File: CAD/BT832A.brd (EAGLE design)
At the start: 22.4 x 43.2 mm, 22 parts, among them IC1 CP2102, U2 BT832, U3 LP5907MFX-3.3/NOPB, U4 LP5907MFX-3.3/NOPB, U5 ADS131M08IPBS, X1_8.192MHZ ABM3B-8.000MHZ-B2-T, X2_32.768KHZ FC-12M

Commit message: finished sch
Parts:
- added C10: 1.0uF, adafruit:C0603
- added C11: 0.1uF, adafruit:C0603
- added C12, C13: 1uF, adafruit:C0603
- added D1: BAT60J, diode:SOD323_ST
- added D2, D3: BAS40-06, diode:SOT23
- added LED1, LED2: (no value), adafruit:CHIP-LED0603
- added R1: 4.7kΩ, adafruit:R0603
- added R2, R3: 3.3kΩ, adafruit:R0603
- added R4, R7: 10kΩ, adafruit:R0603
- added R5: 47kΩ, adafruit:R0603
- added R6: 2kΩ, adafruit:R0603
- added U1: MCP73831T-3ACI/OT, MCP73831T-3ACI_OT:SOT95P270X145-5N
- added U6: BCM857BS, BCM857BS:SOT363_NEX
- moved U3 10.4 mm to (22.3, -5.92)
- moved IC1 5.16 mm to (26.5, -19.0)
- moved C1 2.26 mm to (11.0, -7.92)
- moved C2 2.26 mm to (15.1, -7.92)
- moved X2_32.768KHZ 2.26 mm to (13.1, -7.92)
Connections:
- new net +5V: C10.2, C11.2, C7.1, D2.3, IC1.7, IC1.8, U$1.1, U4.1, U4.3, U6.1
- new net 10K: R4.2, U6.2, U6.5, U6.6
- new net B+: D3.3, J1.2
- new net CPRST: IC1.9, R1.1, U2.B5
- new net D+: IC1.4, U$1.3
- new net D-: IC1.5, U$1.2
- new net ID: U$1.4
- new net N$1: LED2.A, R3.1
- new net N$11: LED1.A, R2.2
- new net N$14: D2.2, R5.1, U6.3
- new net N$18: LED1.C, U1.1
- new net N$2: U2.14
- new net N$3: LED2.C
- new net N$4: U2.9
- new net N$5: R3.2
- new net N$8: U3.2
- new net N$9: R6.1, U1.5
- new net NVD: D1.A, D2.1, D3.2, R2.1, R7.2, U1.4, U6.4
- new net RXD: IC1.25, U2.C5
- new net TXD: IC1.26, U2.D5
- new net VBAT: U1.3
- new net VIN: C13.2, D1.C, D3.1, U3.1, U3.3
- new net VSS: U1.2
- net 3V3: no longer C7.1, U4.1, U4.3
- net GND: now also C10.1, C11.1, C12.1, C13.1, J1.1, R4.1, R5.2, R6.2, R7.1, U$1.5; no longer U3.2
- net VDD: now also C12.2, R1.2, U3.5; no longer U2.9

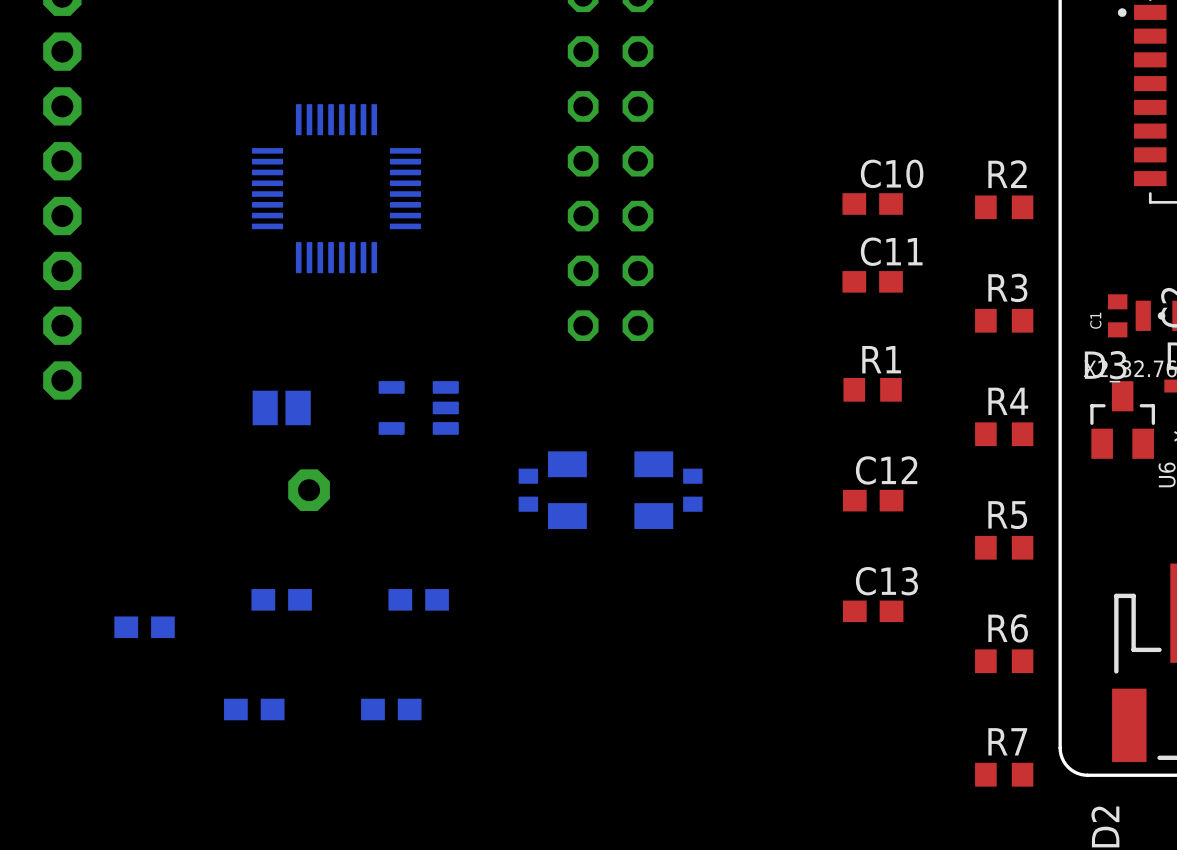
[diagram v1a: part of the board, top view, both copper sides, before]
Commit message: smaller packages
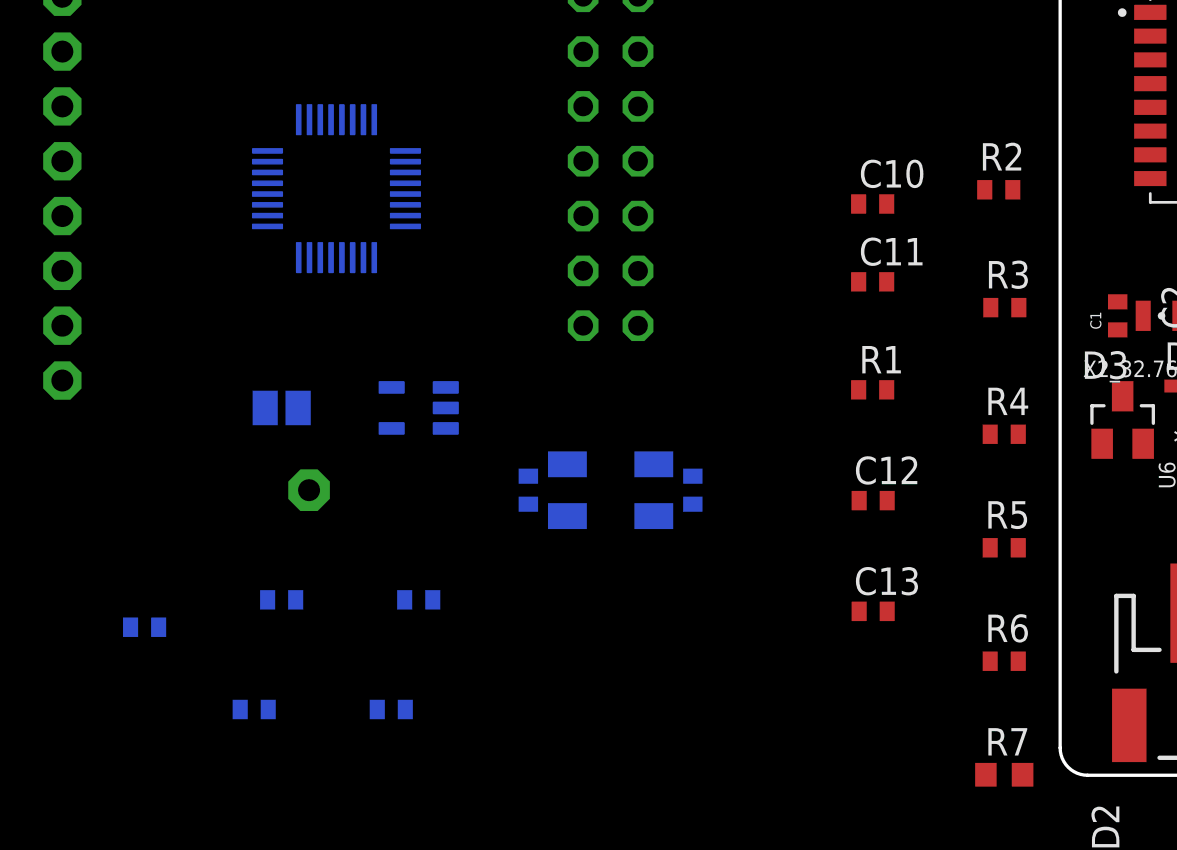
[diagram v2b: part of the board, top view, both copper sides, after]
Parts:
- C10, C11, C12, C13, C5, C6, C7, C8, C9: device adafruit:C0603 -> adafruit:C0402
- R1, R2, R3, R4, R5, R6: device adafruit:R0603 -> adafruit:R0402
- moved R2 0.85 mm to (5.54, -2.08)
- moved R3 0.61 mm to (5.82, -7.54)

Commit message: edits
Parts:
- removed X2_32.768KHZ: FC-12M, crystal:FC-12M
- added X2: FC-12M, crystal:FC-12M
- moved U$2 47.6 mm to (9.73, 0.86)
- moved LED2 29.5 mm to (18.5, -5.23), turned to 90 degrees
- moved R2 25.6 mm to (21.9, -21.7), turned to 90 degrees
- moved R7 21.7 mm to (19.1, -12.0)
- moved R5 13.6 mm to (19.4, -19.0)
- moved R3 13.2 mm to (18.5, -3.91)
- moved LED1 12.8 mm to (20.5, -21.7)
- moved C1 5.88 mm to (16.0, -4.67), turned to 270 degrees
- moved D3 5.36 mm to (11.2, -18.1), turned to 180 degrees
- moved D2 4.78 mm to (14.2, -11.2), turned to 180 degrees
- moved D1 4.75 mm to (18.8, -8.48), turned to 270 degrees
- moved C2 4.56 mm to (11.9, -4.67), turned to 270 degrees
- moved U1 4.26 mm to (15.7, -15.8), turned to 90 degrees
- moved U6 3.74 mm to (19.2, -15.7), turned to 90 degrees
- moved IC1 3.34 mm to (24.4, -16.4)
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- renumbered X1_8.192MHZ to X1
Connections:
- new net SWDCLK: U2.15
- new net SWDIO: U2.16
- net XTAL1_1: now also X2.2; no longer X2_32.768KHZ.2
- net XTAL2_1: now also X2.1; no longer X2_32.768KHZ.1

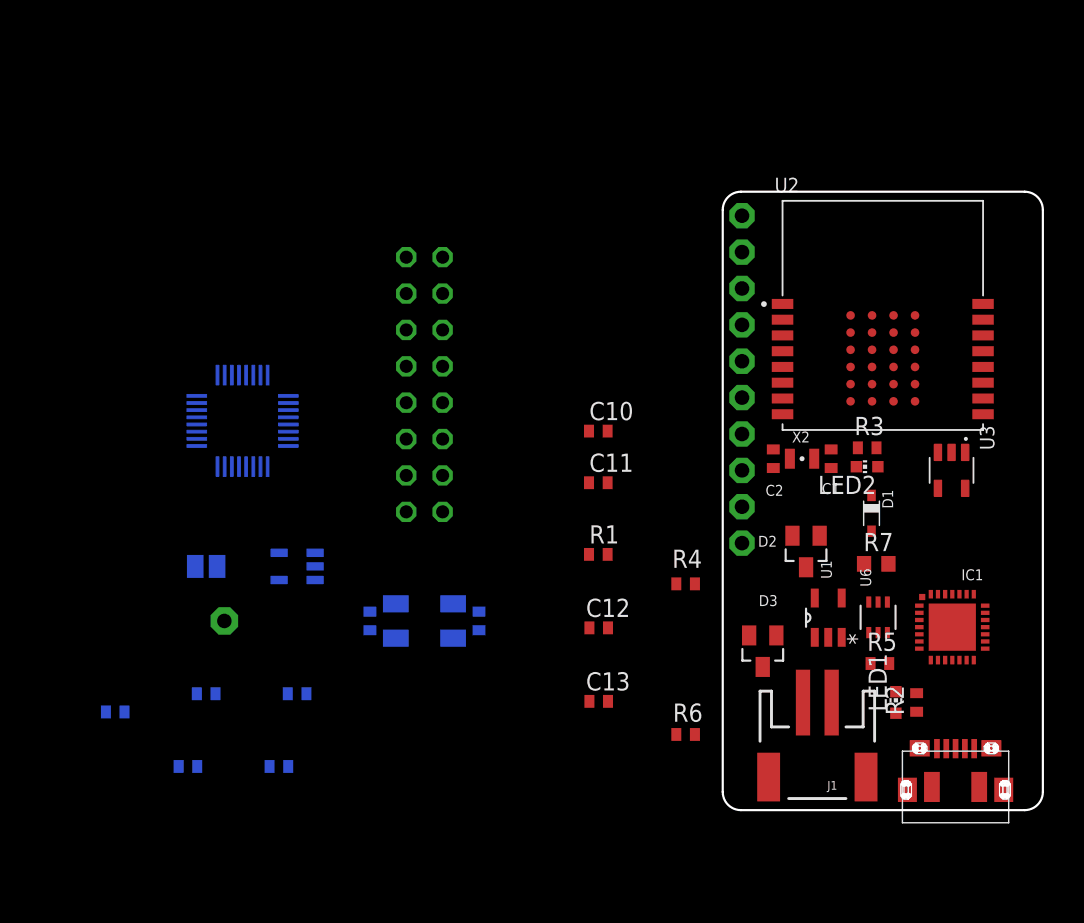
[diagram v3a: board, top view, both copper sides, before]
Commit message: add switch
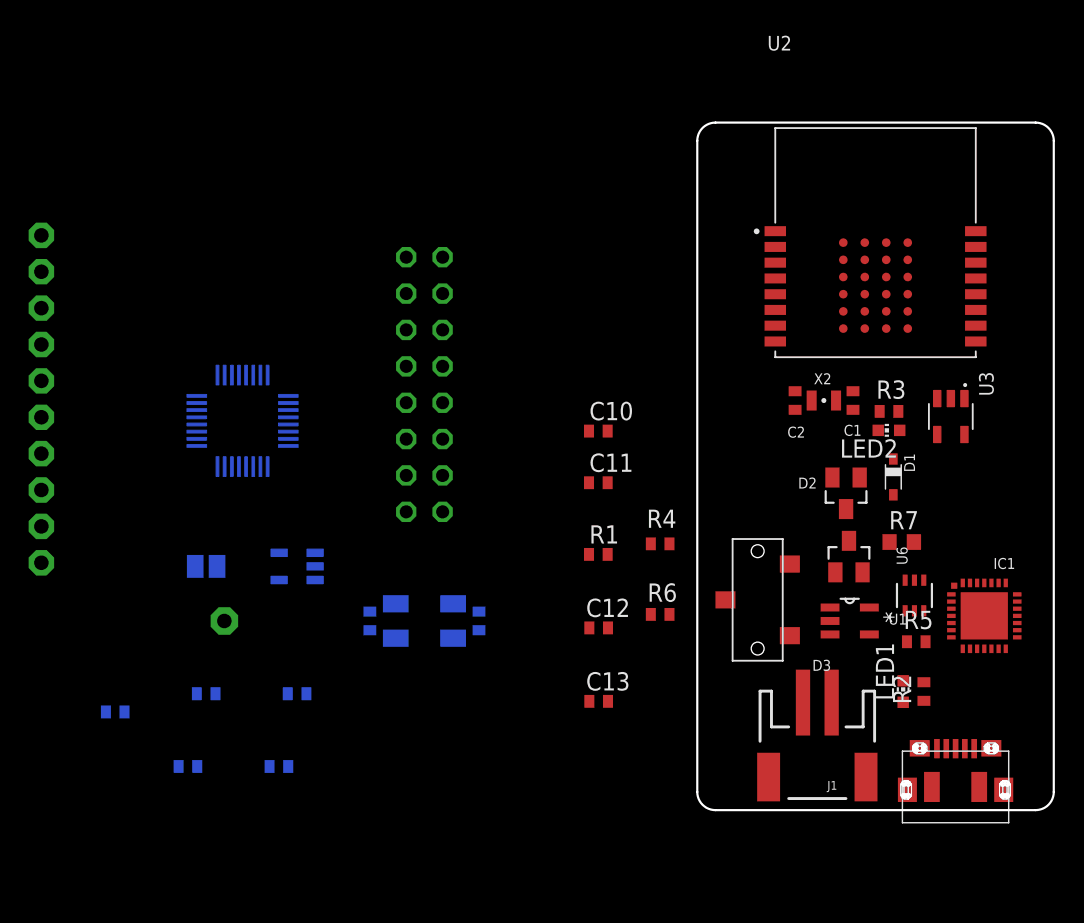
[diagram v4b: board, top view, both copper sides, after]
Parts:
- added S1: CL-SB-12B-01T, CL-SB-12B-01T:CL-SB-12B
- moved U$2 48.9 mm to (-39.2, -0.51)
- moved D3 8.94 mm to (17.2, -11.5), turned to 0 degrees
- moved R6 8.57 mm to (4.01, -15.5)
- moved U2 5.11 mm to (19.1, 10.4)
- moved D2 4.93 mm to (17.0, -7.09)
- moved C1 4.34 mm to (17.5, -0.61)
- moved C2 4.34 mm to (13.4, -0.61)
- moved X2 4.34 mm to (15.4, -0.61)
- moved U3 3.76 mm to (24.3, -1.73)
- moved R4 3.31 mm to (4.01, -10.6)
- moved U6 2.96 mm to (21.8, -14.2)
- moved R5 2.96 mm to (21.9, -17.4)
- moved LED2 2.96 mm to (20.0, -2.69)
- moved R3 2.96 mm to (20.0, -1.37)
- moved D1 2.96 mm to (20.3, -5.94)
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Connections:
- new net D3: D3.3, S1.3
- net B+: now also S1.1; no longer D3.3
- net NC: now also S1.2
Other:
- board size 22.4 x 43.2 mm -> 24.9 x 48 mm

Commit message: edits
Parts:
- moved C10 14.4 mm to (12.9, -8.59)
- moved C12 4.66 mm to (3.78, -18.8)
- moved C11 4.66 mm to (3.76, -8.64)
- moved R1 4.66 mm to (3.76, -13.6)
- moved C13 4.66 mm to (3.78, -23.9)
- moved R4 0.80 mm to (3.76, -11.4)
- moved R6 0.80 mm to (3.76, -16.3)
- moved LED1 0.36 mm to (20.7, -20.7)
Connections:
- net +5V: no longer C7.1, U4.1, U4.3
- net VIN: now also C7.1, U4.1, U4.3

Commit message: edits
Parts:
- moved C12 28.9 mm to (27.7, -2.51), turned to 270 degrees
- moved C13 26.8 mm to (22.1, -4.34)
- moved C11 23.8 mm to (24.9, -19.6), turned to 180 degrees
- moved R1 21.6 mm to (25.1, -10.2), turned to 90 degrees
- moved R4 18.3 mm to (21.0, -17.3), turned to 90 degrees
- moved R6 17.7 mm to (20.8, -11.5)
- moved C10 17.2 mm to (24.9, -20.9), turned to 180 degrees
- moved D2 10.7 mm to (18.3, -17.8)
- moved R2 7.39 mm to (18.1, -14.9), turned to 180 degrees
- moved LED1 7.19 mm to (15.4, -15.8)
- moved U1 3.84 mm to (16.7, -12.2)
- moved D3 3.64 mm to (16.4, -7.95)
- moved D1 1.95 mm to (20.7, -7.85), turned to 180 degrees
- moved U3 1.10 mm to (25.2, -2.34), turned to 90 degrees
- moved R7 0.92 mm to (20.8, -9.58), turned to 180 degrees
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
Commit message: edits
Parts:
- removed R1: 4.7kΩ, adafruit:R0402
- moved C12 5.58 mm to (22.3, -1.04), turned to 90 degrees
- moved C1 1.35 mm to (16.9, -1.83)
- moved C2 1.35 mm to (12.9, -1.83)
- moved X2 1.35 mm to (14.9, -1.83)
- moved C11 0.41 mm to (24.5, -19.6)
- moved C10 0.39 mm to (24.6, -20.8)
- moved D2 0.38 mm to (18.4, -17.4), turned to 270 degrees
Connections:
- removed net VBAT: U1.3
- removed net VSS: U1.2
- net B+: now also U1.3
- net CPRST: no longer R1.1
- net GND: now also U1.2
- net VDD: no longer R1.2
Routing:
- net CPRST: track 0.00 -> 35.5 mm
- net +5V: track 0.00 -> 26.7 mm
- net NVD: track 0.00 -> 14.1 mm
- net VIN: track 0.00 -> 14.0 mm
- net D+: track 0.00 -> 11.1 mm, vias 0 -> 2
- net B+: track 0.00 -> 10.2 mm
- net D-: track 0.00 -> 9.88 mm, vias 0 -> 2
- net D3: track 0.00 -> 7.85 mm
- net N$18: track 0.00 -> 5.23 mm
- net N$11: track 0.00 -> 2.84 mm
- net VDD: track 0.00 -> 2.23 mm
- net N$9: track 0.00 -> 2.11 mm
- net GND: track 0.00 -> 1.99 mm
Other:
- board text removed: "Layer 2"
- board text removed: "Layer 3"

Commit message: edits
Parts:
- moved LED2 9.08 mm to (27.9, 1.78), turned to 0 degrees
- moved R3 5.89 mm to (25.4, 0.97), turned to 180 degrees
- moved C2 0.10 mm to (12.8, -1.93), turned to 90 degrees
- turned C1 to 90 degrees
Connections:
- removed net N$3: LED2.C
- removed net N$4: U2.9
- removed net N$5: R3.2
- net GND: now also LED2.C
- net VDD: now also R3.2, U2.9
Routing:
- net N$14: track 0.00 -> 11.5 mm, vias 0 -> 2
- net NVD: track 14.1 -> 19.0 mm
- net 10K: track 0.00 -> 4.47 mm
